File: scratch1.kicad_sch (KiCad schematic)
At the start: 1 part, among them U1 ATmega32U4-A

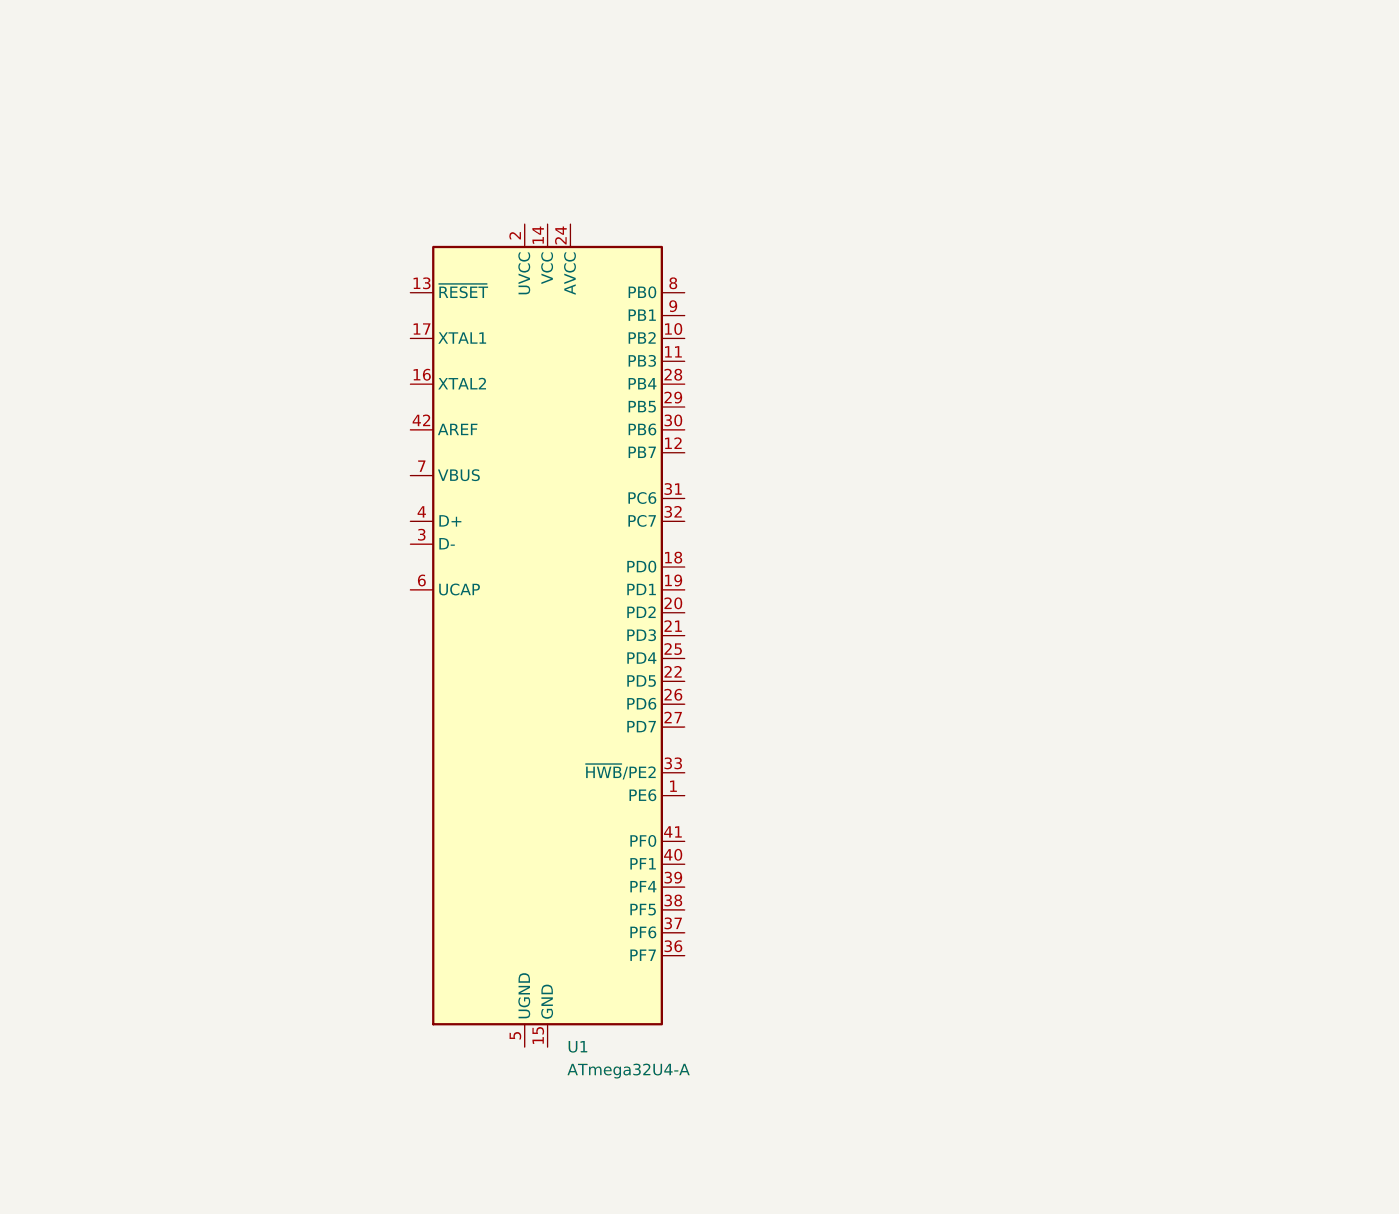
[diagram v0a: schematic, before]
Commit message: complete MCU zone schema
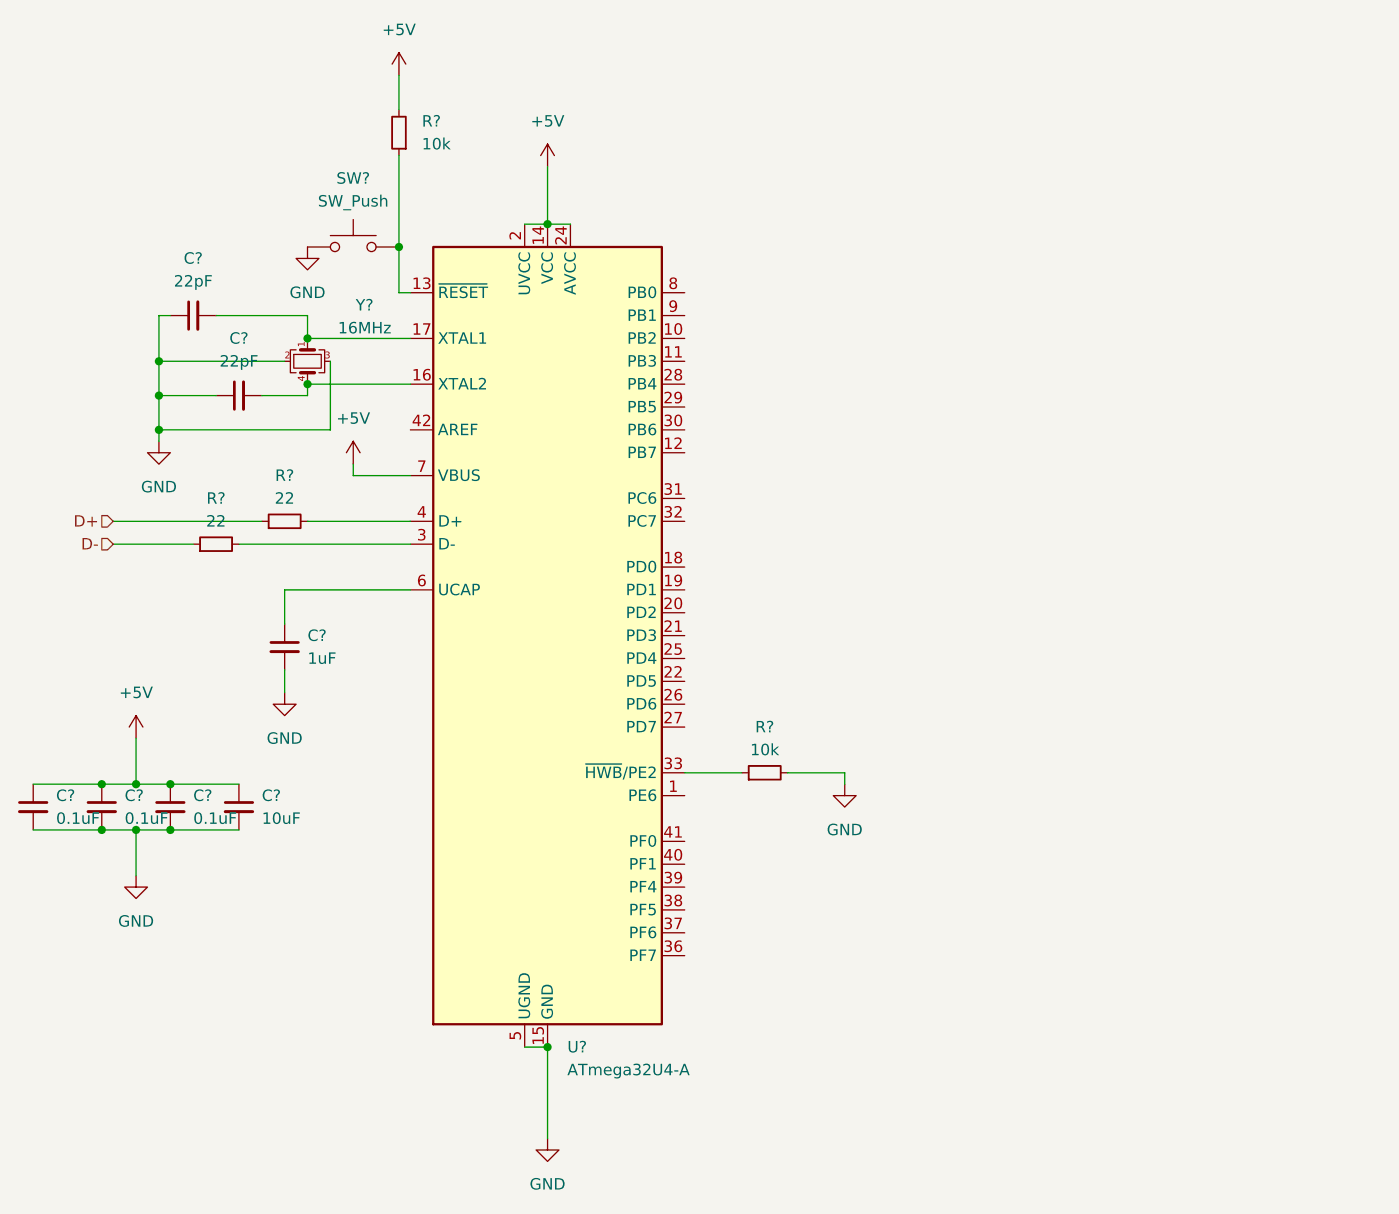
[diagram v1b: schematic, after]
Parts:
- added C?: 10uF, symbol Device:C_Small
- added C? (x3): 0.1uF, symbol Device:C_Small
- added C? (x2): 22pF, symbol Device:C_Small
- added C?: 1uF, symbol Device:C_Small
- added R? (x2): 22, symbol Device:R_Small
- added R? (x2): 10k, symbol Device:R_Small
- added SW?: SW_Push, symbol Switch:SW_Push
- added Y?: 16MHz, symbol Device:Crystal_GND23_Small
- renumbered U1 to U?
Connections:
- net at U?.13 (~{RESET}): now also R?.1, SW?.2
- net +5V: now reaches U?.14 (VCC), U?.34 (VCC)
- net +5V: now also U?.2 (UVCC), U?.24 (AVCC), U?.44 (AVCC), U?.7 (VBUS), C?.1, C?.1, C?.1, C?.1, R?.2
- net GND: now reaches U?.15 (GND), U?.23 (GND), U?.35 (GND), U?.43 (GND)
- net GND: now also U?.5 (UGND), C?.1, C?.1, C?.2, C?.2, C?.2, C?.2, C?.2, R?.2, SW?.1, Y?.2, Y?.3
- net at U?.16 (XTAL2): now also C?.2, Y?.4
- net at U?.17 (XTAL1): now also C?.2, Y?.1
- net at U?.3 (D-): now also R?.2
- net at U?.33 (~{HWB}/PE2): now also R?.1
- net at U?.4 (D+): now also R?.2
- net at U?.6 (UCAP): now also C?.1
- new net D+: R?.1
- new net D-: R?.1

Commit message: complete schema
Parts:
- added D1, D2, D3, D4: 1N4148WS, Diode_SMD:D_SOD-323, symbol Diode:1N4148WS
- added F1: 500mA, symbol Device:Polyfuse
- added J1: USB_B_Micro, symbol Connector:USB_B_Micro
- added MX1, MX2, MX3, MX4: MX-NoLED, symbol MX_Alps_Hybrid:MX-NoLED
- gave numbers to parts that had none: 14
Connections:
- net +5V: now also F1.2
- net D+: now also J1.3 (D+)
- net D-: now also J1.2 (D-)
- net GND: now also J1.5 (GND)
- net ROW0: now reaches U1.27 (PD7)
- net ROW0: now also D1.1 (K), D3.1 (K)
- net COL1: now reaches U1.28 (PB4)
- net COL1: now also MX3.1 (COL), MX4.1 (COL)
- net COL0: now reaches U1.29 (PB5)
- net COL0: now also MX1.1 (COL), MX2.1 (COL)
- net ROW1: now reaches U1.30 (PB6)
- net ROW1: now also D2.1 (K), D4.1 (K)
- new net: D2.2 (A), MX2.2 (ROW)
- new net: D4.2 (A), MX4.2 (ROW)
- new net: D3.2 (A), MX3.2 (ROW)
- new net: D1.2 (A), MX1.2 (ROW)
- new net VCC: F1.1, J1.1 (VBUS)

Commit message: assined footprints
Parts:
- C1, C2, C3, C4, C5, C6, C7: footprint (none) -> Capacitor_SMD:C_0805_2012Metric
- F1: footprint (none) -> Fuse:Fuse_1206_3216Metric
- J1: footprint (none) -> random-keyboard-parts:Molex-0548190589
- MX1, MX2, MX3, MX4: footprint (none) -> MX_Only:MXOnly-1U-NoLED
- R1, R2, R3, R4: footprint (none) -> Resistor_SMD:R_0805_2012Metric
- SW1: footprint (none) -> random-keyboard-parts:SKQG-1155865
- Y1: footprint (none) -> Crystal:Crystal_SMD_3225-4Pin_3.2x2.5mm
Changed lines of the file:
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@@
       (effects (font (size 0.508 0.508)))
     )
-    (property "Footprint" "" (at 178.435 107.315 0)
+    (property "Footprint" "MX_Only:MXOnly-1U-NoLED" (at 178.435 107.315 0)
       (effects (font (size 1.524 1.524)) hide)
     )
@@
       (effects (font (size 1.27 1.27)))
     )
-    (property "Footprint" "" (at 104.14 88.9 0)
+    (property "Footprint" "Resistor_SMD:R_0805_2012Metric" (at 104.14 88.9 0)
       (effects (font (size 1.27 1.27)) hide)
     )
@@
       (effects (font (size 1.27 1.27)))
     )
-    (property "Footprint" "" (at 111.76 86.36 0)
+    (property "Footprint" "Resistor_SMD:R_0805_2012Metric" (at 111.76 86.36 0)
       (effects (font (size 1.27 1.27)) hide)
     )
@@
       (effects (font (size 1.27 1.27)))
     )
-    (property "Footprint" "" (at 114.3 68.58 0)
+    (property "Footprint" "Crystal:Crystal_SMD_3225-4Pin_3.2x2.5mm" (at 114.3 68.58 0)
       (effects (font (size 1.27 1.27)) hide)
     )
@@
       (effects (font (size 1.27 1.27)) (justify left))
     )
-    (property "Footprint" "" (at 106.68 118.11 0)
+    (property "Footprint" "Capacitor_SMD:C_0805_2012Metric" (at 106.68 118.11 0)
       (effects (font (size 1.27 1.27)) hide)
     )
@@
       (effects (font (size 1.27 1.27)))
     )
-    (property "Footprint" "" (at 165.1 114.3 0)
+    (property "Footprint" "Resistor_SMD:R_0805_2012Metric" (at 165.1 114.3 0)
       (effects (font (size 1.27 1.27)) hide)
     )
@@
       (effects (font (size 1.27 1.27)))
     )
-    (property "Footprint" "" (at 218.44 39.37 0)
+    (property "Footprint" "Fuse:Fuse_1206_3216Metric" (at 218.44 39.37 0)
       (effects (font (size 1.27 1.27)) (justify left) hide)
     )
@@
       (effects (font (size 1.27 1.27)) (justify left))
     )
-    (property "Footprint" "" (at 83.82 118.11 0)
+    (property "Footprint" "Capacitor_SMD:C_0805_2012Metric" (at 83.82 118.11 0)
       (effects (font (size 1.27 1.27)) hide)
     )
@@
       (effects (font (size 1.27 1.27)) (justify left))
     )
-    (property "Footprint" "" (at 91.44 118.11 0)
+    (property "Footprint" "Capacitor_SMD:C_0805_2012Metric" (at 91.44 118.11 0)
       (effects (font (size 1.27 1.27)) hide)
     )
@@
       (effects (font (size 1.27 1.27)))
     )
-    (property "Footprint" "" (at 106.68 72.39 0)
+    (property "Footprint" "Capacitor_SMD:C_0805_2012Metric" (at 106.68 72.39 0)
       (effects (font (size 1.27 1.27)) hide)
     )
@@
       (effects (font (size 1.27 1.27)))
     )
-    (property "Footprint" "" (at 119.38 50.8 0)
+    (property "Footprint" "random-keyboard-parts:SKQG-1155865" (at 119.38 50.8 0)
       (effects (font (size 1.27 1.27)) hide)
     )
@@
       (effects (font (size 0.508 0.508)))
     )
-    (property "Footprint" "" (at 178.435 83.185 0)
+    (property "Footprint" "MX_Only:MXOnly-1U-NoLED" (at 178.435 83.185 0)
       (effects (font (size 1.524 1.524)) hide)
     )
@@
       (effects (font (size 1.27 1.27)))
     )
-    (property "Footprint" "" (at 101.6 63.5 0)
+    (property "Footprint" "Capacitor_SMD:C_0805_2012Metric" (at 101.6 63.5 0)
       (effects (font (size 1.27 1.27)) hide)
     )
@@
       (effects (font (size 0.508 0.508)))
     )
-    (property "Footprint" "" (at 205.105 83.185 0)
+    (property "Footprint" "MX_Only:MXOnly-1U-NoLED" (at 205.105 83.185 0)
       (effects (font (size 1.524 1.524)) hide)
     )
@@
       (effects (font (size 1.27 1.27)) (justify left))
     )
-    (property "Footprint" "" (at 111.76 100.33 0)
+    (property "Footprint" "Capacitor_SMD:C_0805_2012Metric" (at 111.76 100.33 0)
       (effects (font (size 1.27 1.27)) hide)
     )
@@
       (effects (font (size 1.27 1.27)) (justify right))
     )
-    (property "Footprint" "" (at 124.46 43.18 0)
+    (property "Footprint" "Resistor_SMD:R_0805_2012Metric" (at 124.46 43.18 0)
       (effects (font (size 1.27 1.27)) hide)
     )
@@
       (effects (font (size 0.508 0.508)))
     )
-    (property "Footprint" "" (at 205.105 107.315 0)
+    (property "Footprint" "MX_Only:MXOnly-1U-NoLED" (at 205.105 107.315 0)
       (effects (font (size 1.524 1.524)) hide)
     )
@@
       (effects (font (size 1.27 1.27)) (justify left))
     )
-    (property "Footprint" "" (at 99.06 118.11 0)
+    (property "Footprint" "Capacitor_SMD:C_0805_2012Metric" (at 99.06 118.11 0)
       (effects (font (size 1.27 1.27)) hide)
     )
@@
       (effects (font (size 1.27 1.27)))
     )
-    (property "Footprint" "" (at 195.58 46.99 0)
-      (effects (font (size 1.27 1.27)) hide)
-    )
+    (property "Footprint" "random-keyboard-parts:Molex-0548190589" (at 195.58 46.99 0)
+      (effects (font (size 1.27 1.27)) hide)
+    )
